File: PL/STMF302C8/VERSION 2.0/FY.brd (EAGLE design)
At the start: 80 x 80 mm, 64 parts, among them J1 CON-SD-CARD_MICROSD-2908-05, J4 FEMALE 2x3, U1 AS72652-BLGT, U2 AS72653-BLGT, U4 AS72651-BLGT, U5 AMS1117-3.3, U6 4MB Flash, U7 MS561101BA03-50, X1 JST-XH-04-PIN-LONG-PAD, Y2 ABM2B-8.000MHZ-10-1-U-T

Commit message: distance holl was putted
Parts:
- removed LS2: CMT-8530S-SMT, SMT-BUZZER:CUI_CMT-8530S-SMT
- added LS1: CMT-7525S-SMT, CMT-7525S-SMT:CUI_CMT-7525S-SMT
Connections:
- net GND: now also LS1.N; no longer LS2.N
- net N$9: now also LS1.P; no longer LS2.P
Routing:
- net N$9: track 5.42 -> 4.20 mm
- net 3.3V: track 371.4 -> 370.4 mm
- added copper zone on layer 1, net D1
- added copper zone on layer 16, net D1
- added copper zone on layer 1, net D2
- added copper zone on layer 16, net D2
- added copper zone on layer 1, net D3
- added copper zone on layer 16, net D3

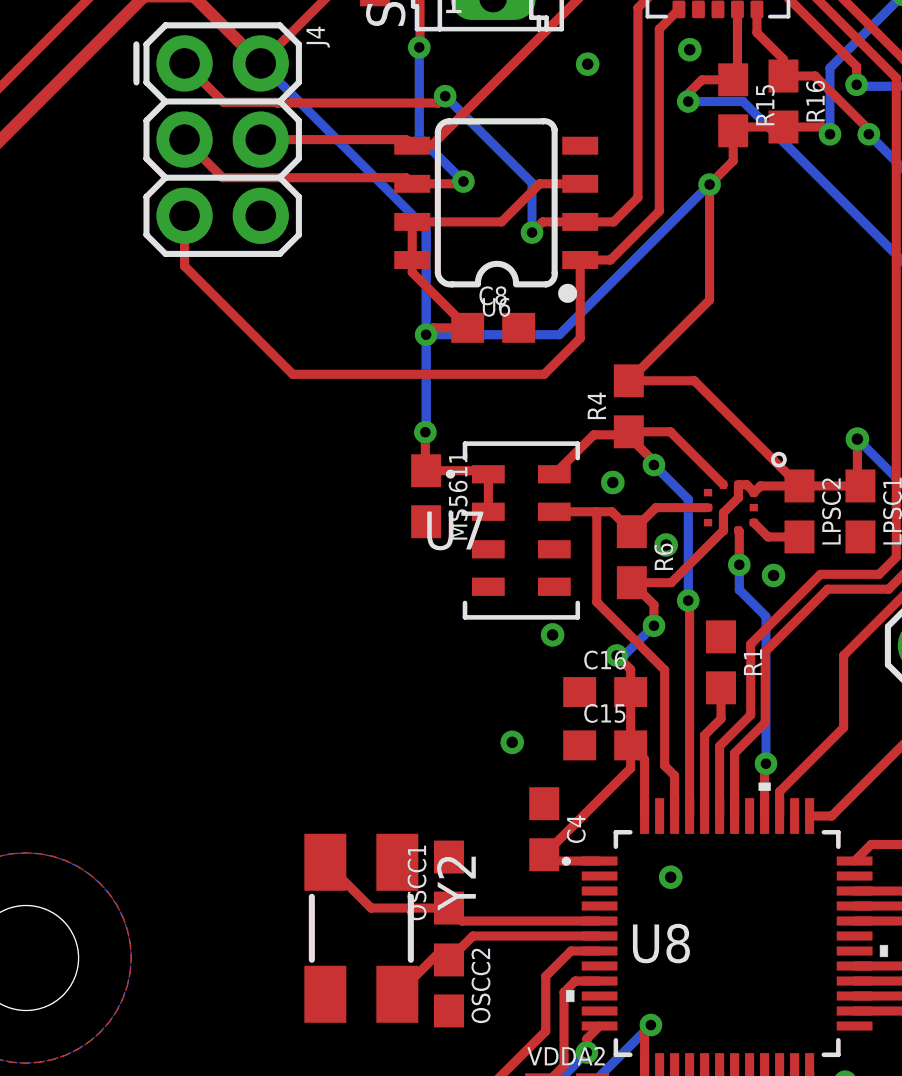
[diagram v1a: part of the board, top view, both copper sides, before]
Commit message: Magnetometer was added by brain.dll
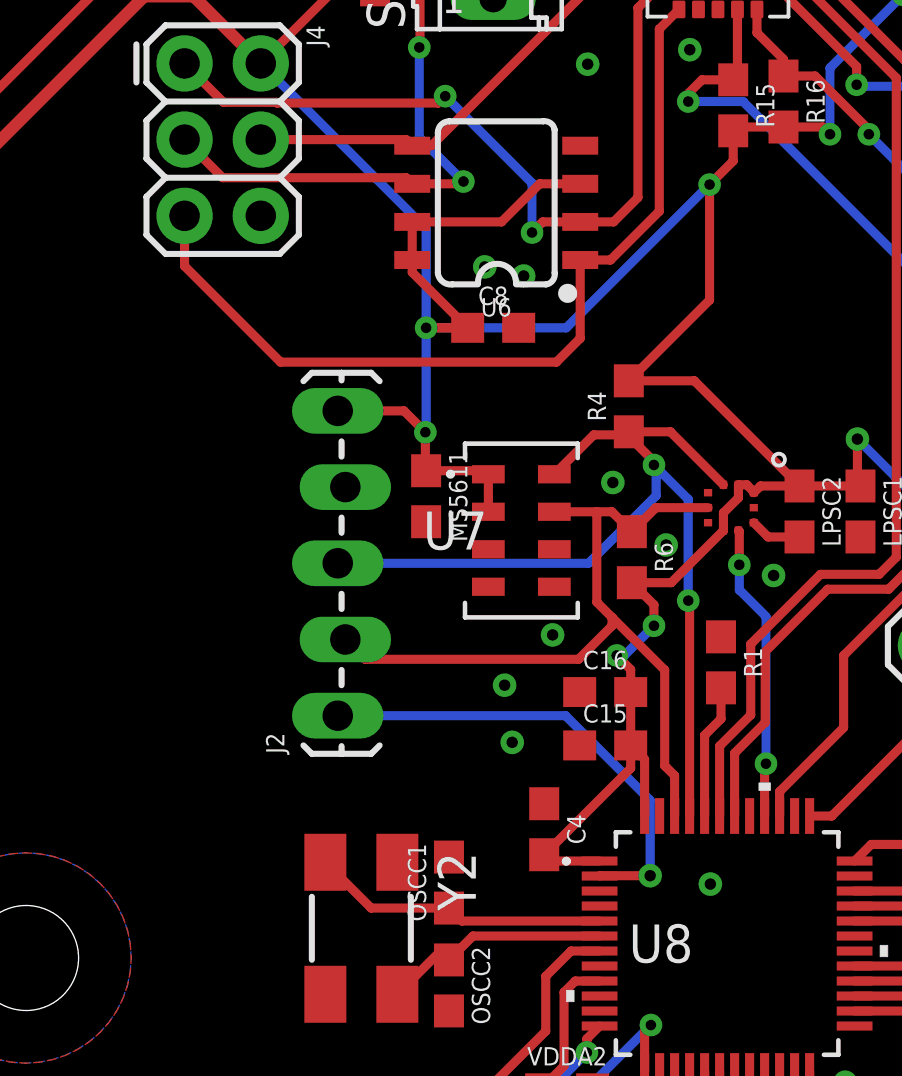
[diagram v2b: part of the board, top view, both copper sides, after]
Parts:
- added J2: (no value), SparkFun-Connectors:1X05_LOCK_LONGPADS
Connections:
- new net DRDY: J2.1, U8.2
- net 3.3V: now also J2.5
- net GND: now also J2.4
- net SCL: now also J2.3
- net SDA: now also J2.2
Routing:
- net DRDY: track 0.00 -> 15.8 mm, vias 0 -> 1
- net SCL: track 20.7 -> 33.3 mm
- net SDA: track 16.9 -> 26.9 mm
- net 3.3V: track 370.4 -> 373.5 mm
- net GND: vias 11 -> 14
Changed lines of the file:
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@@
 <attribute name="VALUE" x="62.23176875" y="36.756340625" size="1.271259375" layer="27" rot="R180"/>
+</element>
+<element name="J2" library="SparkFun-Connectors" library_urn="urn:adsk.eagle:library:513" package="1X05_LOCK_LONGPADS" package3d_urn="urn:adsk.eagle:package:38107/1" value="" x="44.5008" y="51.7652" smashed="yes" rot="R90">
+<attribute name="NAME" x="42.7228" y="50.4952" size="0.6096" layer="25" font="vector" ratio="20" rot="R90"/>
+<attribute name="VALUE" x="46.9138" y="50.3682" size="0.6096" layer="27" font="vector" ratio="20" rot="R90"/>
 </element>
 </elements>
@@
 <via x="52.832" y="73.4822" extent="1-16" drill="0.381"/>
 <via x="50.3174" y="50.8762" extent="1-16" drill="0.381"/>
-<via x="55.6006" y="46.3804" extent="1-16" drill="0.381"/>
+<via x="56.9214" y="46.1518" extent="1-16" drill="0.381"/>
 <contactref element="LS1" pad="N"/>
+<contactref element="J2" pad="4"/>
+<via x="50.0634" y="52.7812" extent="1-16" drill="0.381"/>
+<via x="49.403" y="66.7258" extent="1-16" drill="0.381"/>
+<via x="50.6984" y="66.421" extent="1-16" drill="0.381"/>
 </signal>
 <signal name="3.3V" class="1">
@@
 <wire x1="49.9618" y1="68.2244" x2="51.2318" y2="69.4944" width="0.3048" layer="1"/>
 <wire x1="41.9354" y1="73.5076" x2="47.4472" y2="67.9958" width="0.3048" layer="16"/>
-<wire x1="47.4472" y1="67.9958" x2="47.4472" y2="64.4652" width="0.3048" layer="16"/>
-<via x="47.4472" y="64.4652" extent="1-16" drill="0.35"/>
-<wire x1="47.4472" y1="64.4652" x2="47.6758" y2="64.6938" width="0.3048" layer="1"/>
-<wire x1="47.6758" y1="64.6938" x2="48.8324" y2="64.6938" width="0.3048" layer="1"/>
-<wire x1="47.4472" y1="64.4652" x2="51.8922" y2="64.4652" width="0.3048" layer="16"/>
-<wire x1="51.8922" y1="64.4652" x2="56.896" y2="69.469" width="0.3048" layer="16"/>
+<wire x1="47.4472" y1="67.9958" x2="47.4472" y2="64.6938" width="0.3048" layer="16"/>
+<via x="47.4472" y="64.6938" extent="1-16" drill="0.35"/>
+<wire x1="47.4472" y1="64.6938" x2="48.8324" y2="64.6938" width="0.3048" layer="1"/>
+<wire x1="47.4472" y1="64.6938" x2="52.1208" y2="64.6938" width="0.3048" layer="16"/>
+<wire x1="52.1208" y1="64.6938" x2="56.896" y2="69.469" width="0.3048" layer="16"/>
 <via x="56.896" y="69.469" extent="1-16" drill="0.35"/>
 <wire x1="56.896" y1="69.469" x2="57.6834" y2="70.2564" width="0.3048" layer="1"/>
@@
 <wire x1="56.896" y1="69.469" x2="56.896" y2="65.62" width="0.3048" layer="1"/>
 <wire x1="56.896" y1="65.62" x2="54.2036" y2="62.9276" width="0.3048" layer="1"/>
-<wire x1="47.4472" y1="64.4652" x2="47.4472" y2="61.2394" width="0.3048" layer="16"/>
+<wire x1="47.4472" y1="64.6938" x2="47.4472" y2="61.2394" width="0.3048" layer="16"/>
 <wire x1="47.4472" y1="61.2394" x2="47.4218" y2="61.214" width="0.3048" layer="16"/>
 <via x="47.4218" y="61.214" extent="1-16" drill="0.35"/>
@@
 <wire x1="61.4172" y1="38.696" x2="60.5028" y2="37.7816" width="0.3048" layer="1"/>
 <wire x1="30.1752" y1="18.785246875" x2="37.893653125" y2="13.0556" width="0.3048" layer="1"/>
+<contactref element="J2" pad="5"/>
+<wire x1="47.4218" y1="61.214" x2="46.7106" y2="61.9252" width="0.3048" layer="1"/>
+<wire x1="46.7106" y1="61.9252" x2="44.5008" y2="61.9252" width="0.3048" layer="1"/>
 </signal>
 <signal name="INT">
@@
 <contactref element="J4" pad="5"/>
 <wire x1="52.584" y1="66.9544" x2="52.584" y2="64.3442" width="0.3048" layer="1"/>
-<wire x1="52.584" y1="64.3442" x2="51.3842" y2="63.1444" width="0.3048" layer="1"/>
-<wire x1="51.3842" y1="63.1444" x2="43.0022" y2="63.1444" width="0.3048" layer="1"/>
-<wire x1="43.0022" y1="63.1444" x2="39.3954" y2="66.7512" width="0.3048" layer="1"/>
+<wire x1="52.584" y1="64.3442" x2="51.7906" y2="63.5508" width="0.3048" layer="1"/>
+<wire x1="51.7906" y1="63.5508" x2="42.5958" y2="63.5508" width="0.3048" layer="1"/>
+<wire x1="42.5958" y1="63.5508" x2="39.3954" y2="66.7512" width="0.3048" layer="1"/>
 <wire x1="39.3954" y1="66.7512" x2="39.3954" y2="68.4276" width="0.3048" layer="1"/>
 <wire x1="55.8754" y1="75.3076" x2="55.2196" y2="74.6518" width="0.3048" layer="1"/>
@@
 <wire x1="55.0418" y1="60.237" x2="54.1528" y2="61.126" width="0.3048" layer="1"/>
 <wire x1="54.1528" y1="61.126" x2="54.0512" y2="61.2276" width="0.3048" layer="1"/>
+<contactref element="J2" pad="3"/>
+<wire x1="44.5008" y1="56.8452" x2="52.8574" y2="56.8452" width="0.3048" layer="16"/>
+<wire x1="52.8574" y1="56.8452" x2="55.118" y2="59.1058" width="0.3048" layer="16"/>
+<wire x1="55.118" y1="59.1058" x2="55.118" y2="60.0456" width="0.3048" layer="16"/>
+<wire x1="55.118" y1="60.0456" x2="55.0418" y2="60.1218" width="0.3048" layer="16"/>
 </signal>
 <signal name="SDA">
@@
 <wire x1="55.7302" y1="49.7668" x2="55.7302" y2="48.4206" width="0.3048" layer="1"/>
 <wire x1="55.7302" y1="49.7668" x2="55.4" y2="50.097" width="0.3048" layer="1"/>
-<wire x1="53.1368" y1="55.5498" x2="55.4" y2="53.2866" width="0.3048" layer="1"/>
+<wire x1="53.1368" y1="55.5498" x2="53.6448" y2="55.0418" width="0.3048" layer="1"/>
+<contactref element="J2" pad="2"/>
+<wire x1="53.6448" y1="55.0418" x2="55.4" y2="53.2866" width="0.3048" layer="1"/>
+<wire x1="52.5272" y1="53.6448" x2="45.4152" y2="53.6448" width="0.3048" layer="1"/>
+<wire x1="44.7548" y1="54.3052" x2="45.4152" y2="53.6448" width="0.3048" layer="1"/>
+<wire x1="52.5272" y1="53.6448" x2="53.6448" y2="54.7624" width="0.3048" layer="1"/>
+<wire x1="53.6448" y1="54.7624" x2="53.6448" y2="55.0418" width="0.3048" layer="1"/>
 </signal>
 <signal name="USB_N">
@@
 </polygon>
 </signal>
+<signal name="DRDY">
+<contactref element="J2" pad="1"/>
+<contactref element="U8" pad="2"/>
+<wire x1="44.5008" y1="51.7652" x2="52.0954" y2="51.7652" width="0.3048" layer="16"/>
+<via x="54.9148" y="46.4312" extent="1-16" drill="0.381"/>
+<wire x1="54.9148" y1="46.4312" x2="53.2408" y2="46.4312" width="0.3048" layer="1"/>
+<wire x1="53.2408" y1="46.4312" x2="53.2302" y2="46.4206" width="0.3048" layer="1"/>
+<wire x1="54.9148" y1="46.4312" x2="54.9148" y2="48.9458" width="0.3048" layer="16"/>
+<wire x1="54.9148" y1="48.9458" x2="52.0954" y2="51.7652" width="0.3048" layer="16"/>
+</signal>
 </signals>

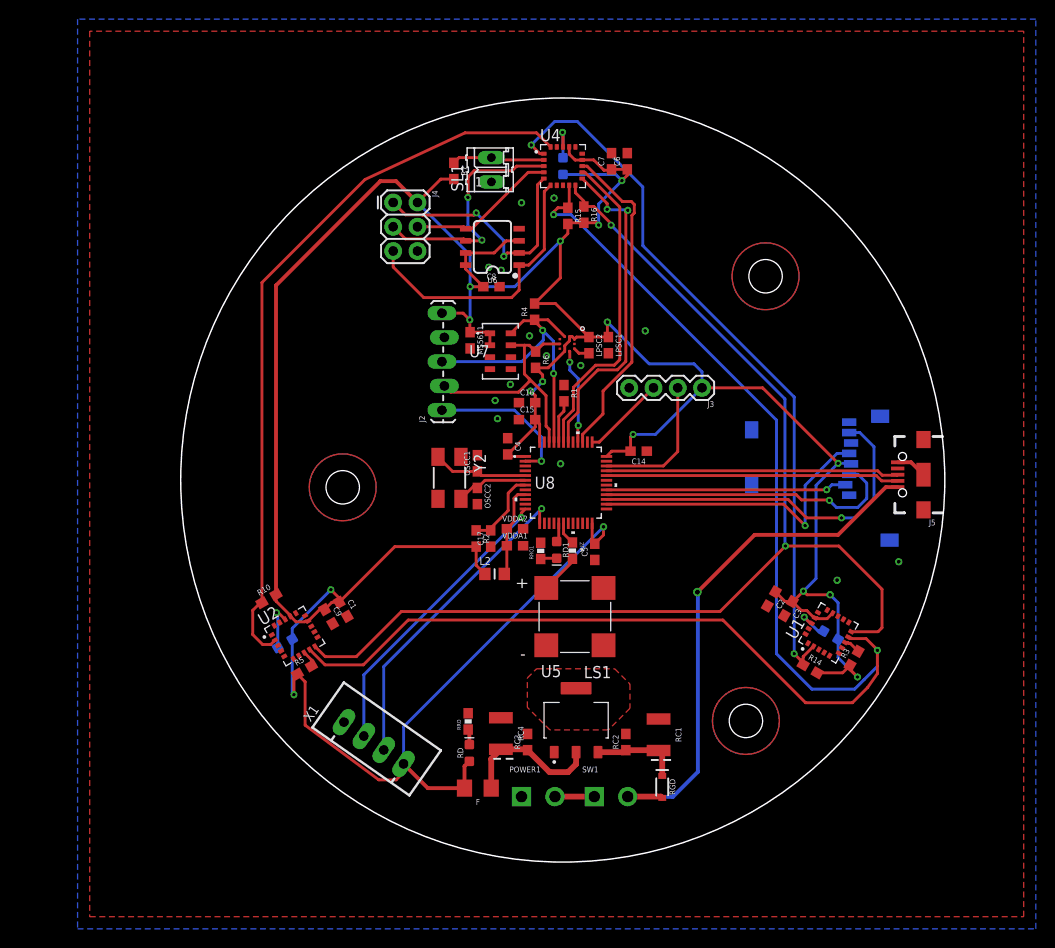
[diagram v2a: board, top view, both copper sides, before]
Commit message: holes were moved and VDDA cap value was changed
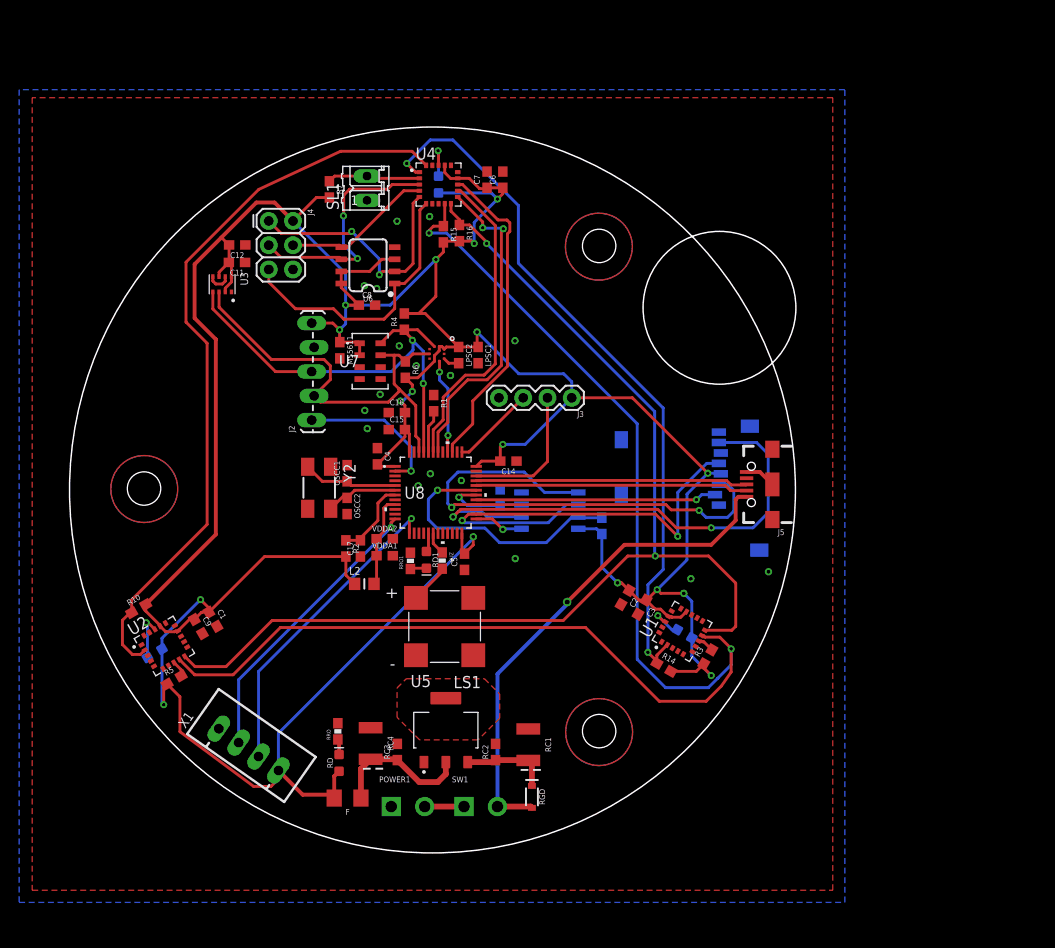
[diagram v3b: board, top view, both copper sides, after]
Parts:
- added C11, C12: 100nF, SparkFun-Capacitors:0603
- added HOLDR, WPR: 10k, SparkFun-Resistors:0603-RES
- added IC1: EN25F40-100GCP-TR, adafruit:SO08-SKINNYPADS
- added U3: BMP280, BMP280:XDCR_BMP280
- VDDA2: value 100nF -> 10nF
- moved J5 15.9 mm to (79.1, 44.0)
- moved C3 15.3 mm to (65.5, 31.1)
- moved R14 15.3 mm to (67.7, 24.8)
- moved C2 15.3 mm to (63.7, 32.2)
- moved D2 15.3 mm to (69.9, 28.3)
- moved R3 15.3 mm to (72.3, 25.9)
- moved U1 15.3 mm to (69.6, 28.6)
- moved J3 13.7 mm to (58.1, 53.1)
- moved RC1 13.7 mm to (53.5, 16.7)
- moved Y2 13.7 mm to (31.6, 43.6)
- moved C9 13.7 mm to (19.0, 29.1)
- moved C14 13.7 mm to (51.5, 46.4)
- moved C15 13.7 mm to (39.8, 49.7)
- moved C17 13.7 mm to (36.0, 37.3)
- moved C4 13.7 mm to (37.7, 46.9)
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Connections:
- new net CSF: IC1.1, U8.25
- new net HOLD: HOLDR.1, IC1.7, U8.31
- new net WP: IC1.3, U8.30, WPR.2
- net 3.3V: now also C11.2, C12.2, HOLDR.2, IC1.8, U3.2, U3.6, U3.8
- net GND: now also C11.1, C12.1, IC1.4, U3.1, U3.5, U3.7, WPR.1
- net MISO: now also IC1.2
- net MOSI: now also IC1.5
- net SCK: now also IC1.6
- net SCL: now also U3.4
- net SDA: now also U3.3
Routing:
- net HOLD: track 0.00 -> 27.9 mm, vias 0 -> 1
- net MOSI: track 32.0 -> 52.3 mm, vias 1 -> 2
- net SDA: track 26.9 -> 46.5 mm
- net 3.3V: track 373.5 -> 390.6 mm, vias 16 -> 17
- net MISO: track 38.3 -> 54.2 mm, vias 1 -> 2
- net SCK: track 31.9 -> 47.0 mm, vias 1 -> 2
- net SCL: track 33.3 -> 48.2 mm
- net WP: track 0.00 -> 8.87 mm, vias 0 -> 1
- net CSF: track 0.00 -> 5.22 mm, vias 0 -> 1
- net SCL_M: track 149.0 -> 144.0 mm
- net VIN: track 56.5 -> 52.8 mm
- net SDA_M: track 121.4 -> 118.4 mm
- net GND: track 4.96 -> 7.45 mm, vias 14 -> 17
- net USB_P: track 30.7 -> 28.5 mm
- net USB_N: track 30.7 -> 28.5 mm
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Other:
- board size 80 x 80 mm -> 76 x 76 mm

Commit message: 05.07.2021
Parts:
- removed LS1: CMT-7525S-SMT, CMT-7525S-SMT:CUI_CMT-7525S-SMT
- added LS2: BUZZER-PTH, SparkFun-Electromechanical:BUZZER-12MM
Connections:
- net GND: now also LS2.-; no longer LS1.N
- net N$9: now also LS2.+; no longer LS1.P
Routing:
- net N$9: track 4.20 -> 9.35 mm
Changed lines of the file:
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@@
 <attribute name="PURCHASE-URL" value="https://pricing.snapeda.com/search/part/ABM3B-26.000MHZ-10-1-U-T/?ref=eda" x="-10.2616" y="-4.6228" size="1.778" layer="27" rot="R270" display="off"/>
-</element>
-<element name="LS1" library="CMT-7525S-SMT" package="CUI_CMT-7525S-SMT" value="CMT-7525S-SMT" x="44.7802" y="29.1084" smashed="yes" rot="R180">
-<attribute name="AVAILABILITY" value="In Stock" x="44.7802" y="29.1084" size="1.778" layer="27" rot="R180" display="off"/>
-<attribute name="CUI_PURCHASE_URL" value="https://www.cuidevices.com/product/audio/buzzers/audio-transducers/cmt-7525s-smt-tr?utm_source=snapeda.com&amp;utm_medium=referral&amp;utm_campaign=snapedaBOM" x="44.7802" y="29.1084" size="1.778" layer="27" rot="R180" display="off"/>
-<attribute name="DESCRIPTION" value="7.5 mm, 3.6 Vo-p, 90 dB, Surface Mount (SMT), Magnetic Audio Transducer Buzzer" x="44.7802" y="29.1084" size="1.778" layer="27" rot="R180" display="off"/>
-<attribute name="MF" value="CUI Devices" x="44.7802" y="29.1084" size="1.778" layer="27" rot="R180" display="off"/>
-<attribute name="MP" value="CMT-7525S-SMT-TR" x="44.7802" y="29.1084" size="1.778" layer="27" rot="R180" display="off"/>
-<attribute name="NAME" x="48.584709375" y="23.932259375" size="1.271509375" layer="25" rot="R180"/>
-<attribute name="PACKAGE" value=" CUI Inc." x="44.7802" y="29.1084" size="1.778" layer="27" rot="R180" display="off"/>
-<attribute name="PRICE" value="None" x="44.7802" y="29.1084" size="1.778" layer="27" rot="R180" display="off"/>
-<attribute name="VALUE" x="48.59196875" y="35.714940625" size="1.271259375" layer="27" rot="R180"/>
 </element>
 <element name="J2" library="SparkFun-Connectors" library_urn="urn:adsk.eagle:library:513" package="1X05_LOCK_LONGPADS" package3d_urn="urn:adsk.eagle:package:38107/1" value="" x="30.861" y="50.7238" smashed="yes" rot="R90">
@@
 <attribute name="PROD_ID" value="CAP-00868" x="31.3944" y="65.8368" size="1.778" layer="27" rot="R180" display="off"/>
 <attribute name="VALUE" x="23.0632" y="69.8246" size="0.6096" layer="27" font="vector" ratio="20" rot="R180" align="top-center"/>
+</element>
+<element name="LS2" library="SparkFun-Electromechanical" library_urn="urn:adsk.eagle:library:516" package="BUZZER-12MM" package3d_urn="urn:adsk.eagle:package:38558/1" value="BUZZER-PTH" x="54.7878" y="29.5148" smashed="yes" rot="R135">
+<attribute name="NAME" x="50.477278125" y="25.204275" size="0.6096" layer="25" font="vector" ratio="20" rot="R135" align="bottom-center"/>
+<attribute name="PROD_ID" value="COMP-08253" x="54.087340625" y="11.787771875" size="1.778" layer="27" rot="R135" display="off"/>
+<attribute name="SF_SKU" value="COM-07950" x="54.087340625" y="11.787771875" size="1.778" layer="27" rot="R135" display="off"/>
+<attribute name="VALUE" x="50.8364875" y="25.563484375" size="0.6096" layer="27" font="vector" ratio="20" rot="R135" align="top-center"/>
 </element>
 </elements>
@@
 <via x="36.6776" y="49.8348" extent="1-16" drill="0.381"/>
 <via x="43.2816" y="45.1104" extent="1-16" drill="0.381"/>
-<contactref element="LS1" pad="N"/>
 <contactref element="J2" pad="4"/>
 <via x="36.4236" y="51.7398" extent="1-16" drill="0.381"/>
@@
 <wire x1="20.5134" y1="65.2878" x2="20.5134" y2="65.7478" width="0.3048" layer="1"/>
 <wire x1="20.828" y1="64.9732" x2="20.5134" y2="65.2878" width="0.3048" layer="1"/>
+<contactref element="LS2" pad="-"/>
 </signal>
 <signal name="3.3V" class="1">
@@
 <wire x1="72.6948" y1="37.6682" x2="63.6016" y2="37.6682" width="0.4064" layer="1"/>
 </signal>
-<signal name="N$9">
-<contactref element="BUZ" pad="2"/>
-<contactref element="LS1" pad="P"/>
-<wire x1="44.5262" y1="35.1672" x2="44.5262" y2="34.8544" width="0.3048" layer="1"/>
-<wire x1="44.5262" y1="34.8544" x2="41.7802" y2="32.1084" width="0.3048" layer="1"/>
-</signal>
 <signal name="N$3">
 <contactref element="POWER1" pad="2"/>
@@
 <wire x1="49.7781" y1="40.3792" x2="48.0904" y2="40.3792" width="0.3048" layer="1"/>
 </signal>
+<signal name="N$9">
+<contactref element="BUZ" pad="2"/>
+<contactref element="LS2" pad="+"/>
+<wire x1="44.5262" y1="35.1672" x2="47.880503125" y2="31.812896875" width="0.3048" layer="1"/>
+<wire x1="47.880503125" y1="31.812896875" x2="52.4897" y2="31.812896875" width="0.3048" layer="1"/>
+</signal>
 </signals>
